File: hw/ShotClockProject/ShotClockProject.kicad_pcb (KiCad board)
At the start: 4 copper layers, 71.8 x 71.8 mm, 113 parts, among them IC1 TP4056-42-ESOP8_Rearanged, J1 Conn_01x06_Pin, J10 USB4120-03-C_REVA, J2 Conn_ST_STDC14, J3 SM03B-SRSS-TB(LF)(SN)(P), J4 Conn_01x02_Pin, J5 Conn_01x03_Pin, J6 Conn_01x06_Pin, J7 Conn_01x06_Pin, J8 Conn_01x06_Pin, J9 Conn_01x06_Pin, Q1 Q_PMOS_SGD, Q2 Q_NPN_BCE, Q3 Q_NPN_BCE, Q4 Q_NPN_BCE, SW1 TK-6580S-1, SW2 SW_SPDT, SW3 TK-6580S-2, SW4 TK-6580S-2, SW5 TK-6580S-2, U1 STM32G070CBTx, U2 LD39015M33R, U3 TPS63000, U4 TPS63000, U5 M74HC14YRM13TR, U6 USBLC6-2SC6, Y1 16MHz

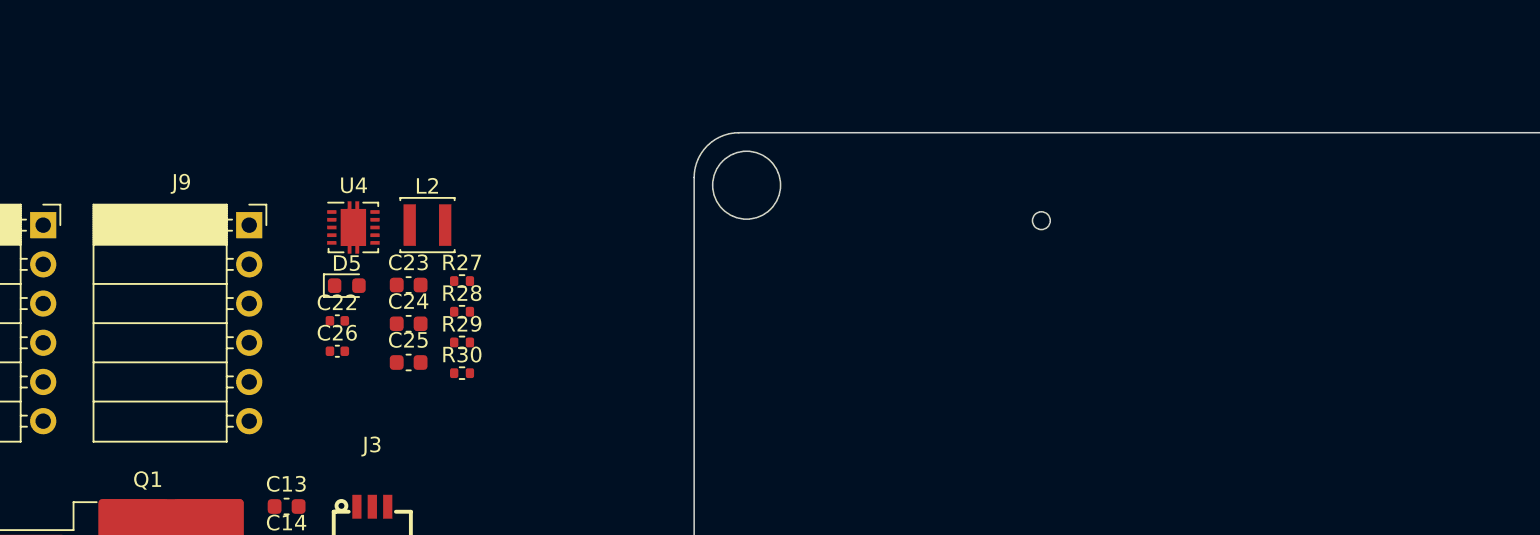
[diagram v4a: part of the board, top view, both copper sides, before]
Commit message: Cleaned second print
and added new connectors, pinout and removed all REV1 stuff.
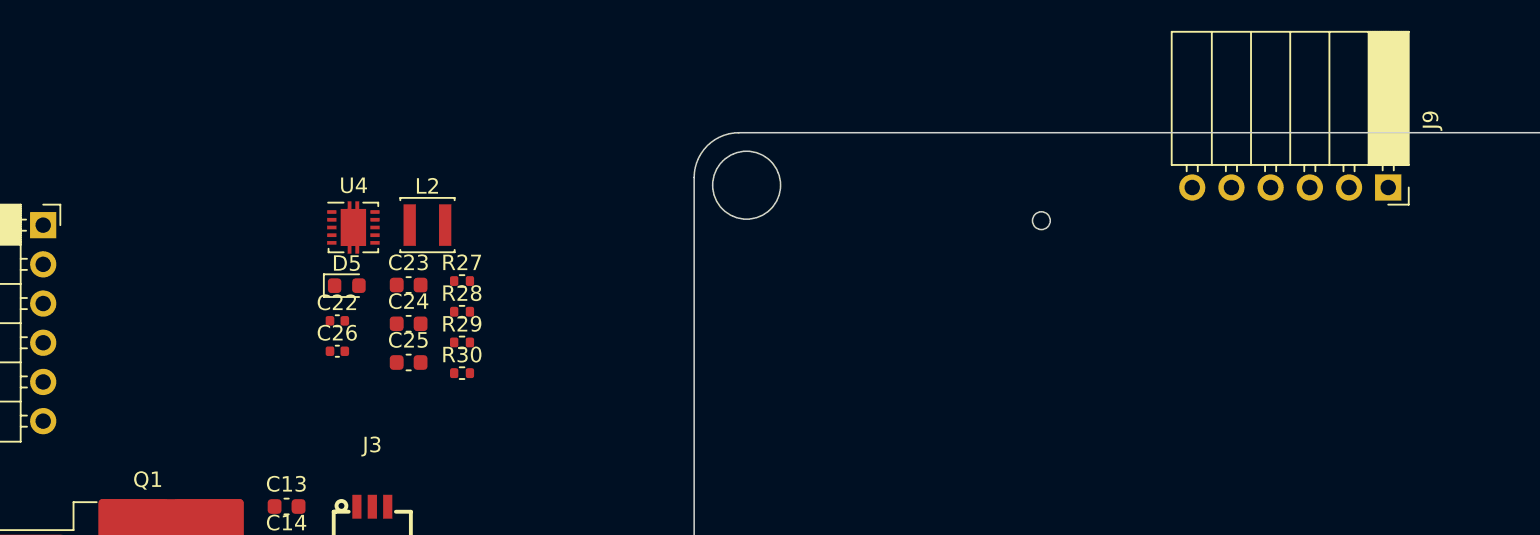
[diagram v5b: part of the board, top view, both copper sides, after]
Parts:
- moved J9 73.8 mm to (163.1, 67.7), turned to -90 degrees
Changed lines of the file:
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@@
   )
   (footprint "Connector_PinSocket_2.54mm:PinSocket_1x06_P2.54mm_Horizontal" (layer "F.Cu")
-    (at 89.27 70.09)
+    (at 163.075 67.65 -90)
     (descr "Through hole angled socket strip, 1x06, 2.54mm pitch, 8.51mm socket length, single row (from Kicad 4.0.7), script generated")
     (tags "Through hole angled socket strip THT 1x06 2.54mm single row")
@@
     (property "ki_keywords" "connector")
     (attr through_hole)
-    (fp_text reference "J9" (at -4.38 -2.77) (layer "F.SilkS")
+    (fp_text reference "J9" (at -4.38 -2.77 90) (layer "F.SilkS")
         (effects (font (size 1 1) (thickness 0.15)))
     )
-    (fp_text value "Conn_01x06_Pin" (at -4.38 15.47) (layer "F.Fab")
+    (fp_text value "Conn_01x06_Pin" (at -4.38 15.47 90) (layer "F.Fab")
         (effects (font (size 1 1) (thickness 0.15)))
     )
-    (fp_text user "${REFERENCE}" (at -5.775 6.35 90) (layer "F.Fab")
+    (fp_text user "${REFERENCE}" (at -5.775 6.35) (layer "F.Fab")
         (effects (font (size 1 1) (thickness 0.15)))
     )
@@
     (fp_line (start 0 13) (end 0 12.4)
       (stroke (width 0.1) (type solid)) (layer "F.Fab"))
-    (pad "1" thru_hole rect (at 0 0) (size 1.7 1.7) (drill 1) (layers "*.Cu" "*.Mask")
+    (pad "1" thru_hole rect (at 0 0 270) (size 1.7 1.7) (drill 1) (layers "*.Cu" "*.Mask")
       (net 53 "TLC59116_RESETn") (pinfunction "Pin_1") (pintype "passive"))
-    (pad "2" thru_hole oval (at 0 2.54) (size 1.7 1.7) (drill 1) (layers "*.Cu" "*.Mask")
+    (pad "2" thru_hole oval (at 0 2.54 270) (size 1.7 1.7) (drill 1) (layers "*.Cu" "*.Mask")
       (net 2 "+3.3V") (pinfunction "Pin_2") (pintype "passive"))
-    (pad "3" thru_hole oval (at 0 5.08) (size 1.7 1.7) (drill 1) (layers "*.Cu" "*.Mask")
+    (pad "3" thru_hole oval (at 0 5.08 270) (size 1.7 1.7) (drill 1) (layers "*.Cu" "*.Mask")
       (net 54 "+5V") (pinfunction "Pin_3") (pintype "passive"))
-    (pad "4" thru_hole oval (at 0 7.62) (size 1.7 1.7) (drill 1) (layers "*.Cu" "*.Mask")
+    (pad "4" thru_hole oval (at 0 7.62 270) (size 1.7 1.7) (drill 1) (layers "*.Cu" "*.Mask")
       (net 55 "I2C1_SCL") (pinfunction "Pin_4") (pintype "passive"))
-    (pad "5" thru_hole oval (at 0 10.16) (size 1.7 1.7) (drill 1) (layers "*.Cu" "*.Mask")
+    (pad "5" thru_hole oval (at 0 10.16 270) (size 1.7 1.7) (drill 1) (layers "*.Cu" "*.Mask")
       (net 56 "I2C1_SDA") (pinfunction "Pin_5") (pintype "passive"))
-    (pad "6" thru_hole oval (at 0 12.7) (size 1.7 1.7) (drill 1) (layers "*.Cu" "*.Mask")
+    (pad "6" thru_hole oval (at 0 12.7 270) (size 1.7 1.7) (drill 1) (layers "*.Cu" "*.Mask")
       (net 4 "GND") (pinfunction "Pin_6") (pintype "passive"))
     (model "${KICAD6_3DMODEL_DIR}/Connector_PinSocket_2.54mm.3dshapes/PinSocket_1x06_P2.54mm_Horizontal.wrl"

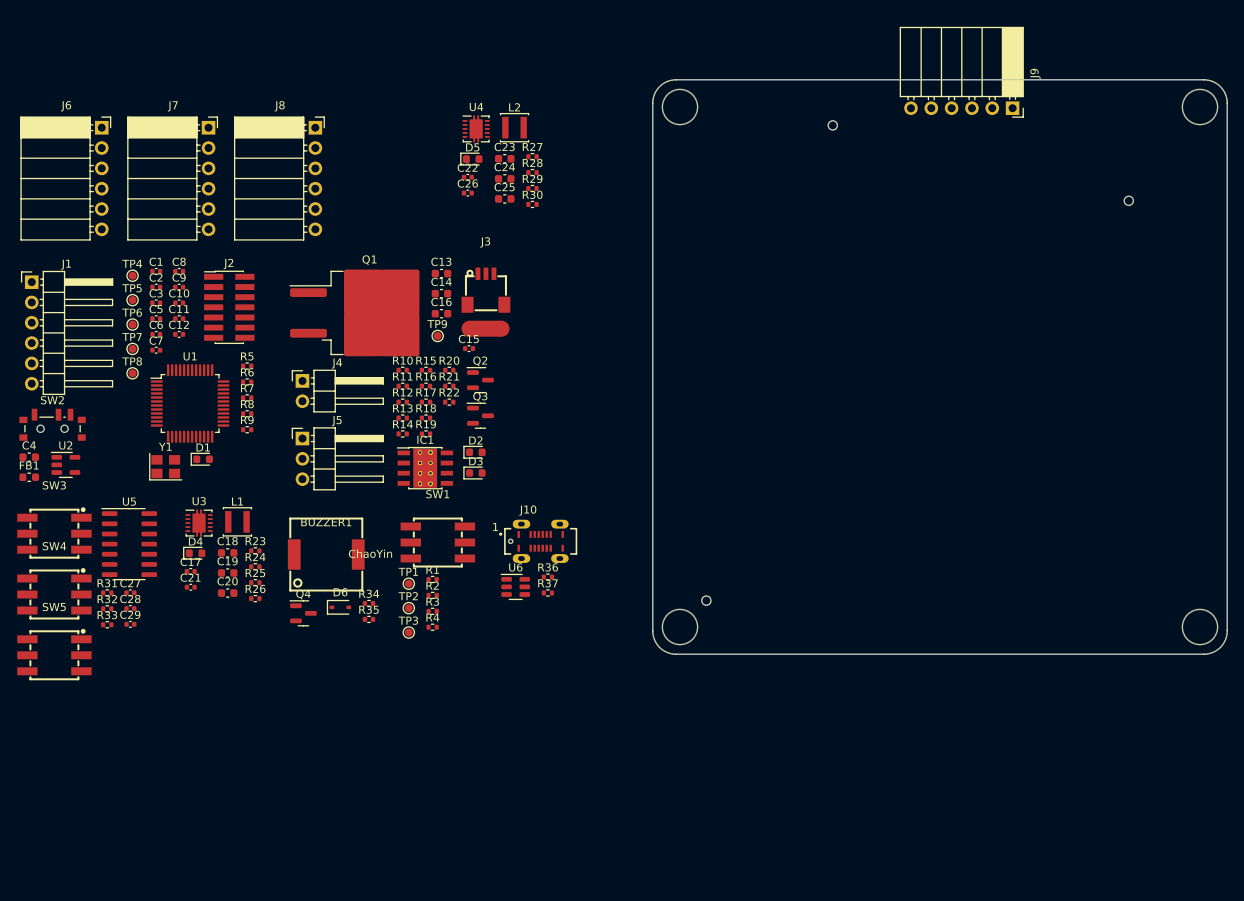
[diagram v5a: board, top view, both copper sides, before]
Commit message: Changed display connectors to JST PH 2.0mm
In docs, schematic and footprints
Both sides, connect with male/male cable
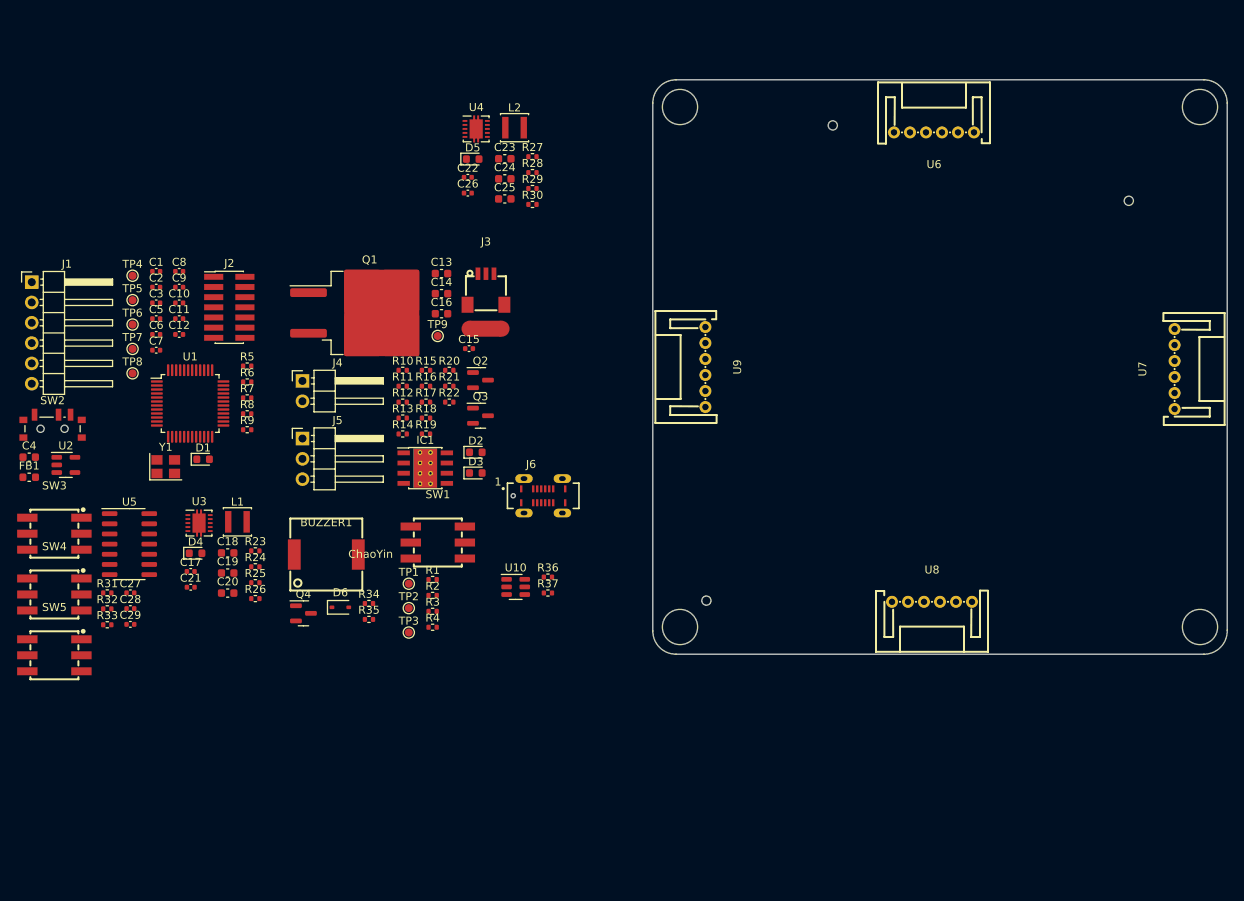
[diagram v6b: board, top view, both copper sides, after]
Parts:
- removed the J6 at (49.2, 70.1)
- removed J7, J8, J9: Conn_01x06_Pin, Connector_PinSocket_2.54mm:PinSocket_1x06_P2.54mm_Horizontal
- added U6: S6B-PH-K-S-(LF)(SN), S6B_PH_K_S_LF_SN:CONN-TH_6P-P2.00_S6B-PH-K-S-LF-SN, F.Cu at (153.2, 70.7)
- added U7: S6B-PH-K-S-(LF)(SN), S6B_PH_K_S_LF_SN:CONN-TH_6P-P2.00_S6B-PH-K-S-LF-SN, F.Cu at (183.3, 100.2)
- added U8: S6B-PH-K-S-(LF)(SN), S6B_PH_K_S_LF_SN:CONN-TH_6P-P2.00_S6B-PH-K-S-LF-SN, F.Cu at (153.0, 129.3)
- added U9: S6B-PH-K-S-(LF)(SN), S6B_PH_K_S_LF_SN:CONN-TH_6P-P2.00_S6B-PH-K-S-LF-SN, F.Cu at (124.7, 100.0)
- moved J6 5.70 mm to (104.4, 116.1)
- renumbered J10 to J6, U6 to U10

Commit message: XTAL, decoup placement & I2C routing
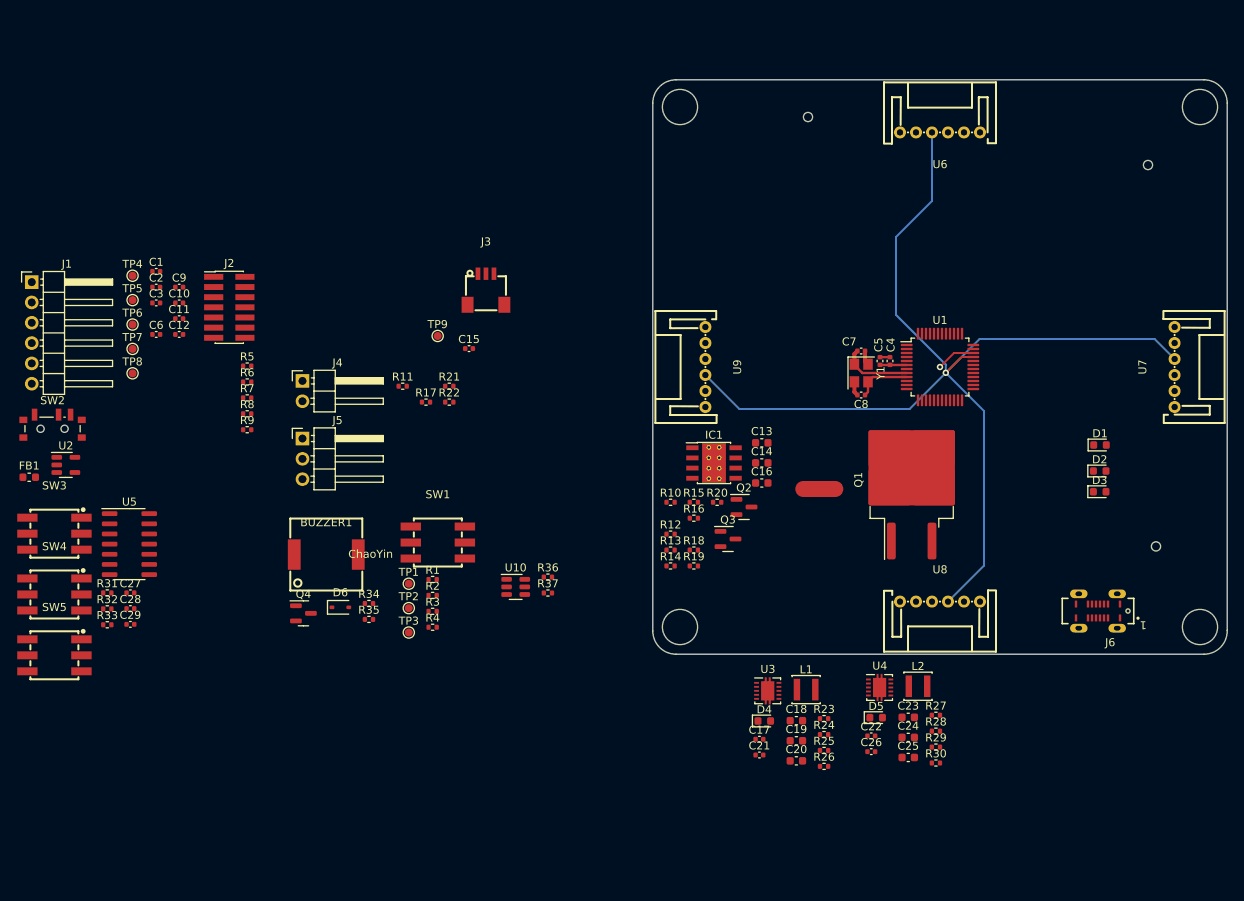
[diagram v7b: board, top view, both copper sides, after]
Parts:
- C4: footprint Capacitor_SMD:C_0603_1608Metric -> Capacitor_SMD:C_0402_1005Metric
- moved D1 112.1 mm to (174.0, 109.8)
- moved C4 108.3 mm to (147.8, 99.2), turned to 90 degrees
- moved U1 93.8 mm to (154.0, 100.0)
- moved C5 90.6 mm to (146.5, 99.2), turned to 90 degrees
- moved C7 88.1 mm to (144.2, 98.0)
- moved Y1 87.7 mm to (144.2, 100.8), turned to -90 degrees
- moved C8 86.6 mm to (144.2, 103.5), turned to 180 degrees
- moved C22 86.1 mm to (145.4, 146.1)
- moved C24 86.1 mm to (150.0, 146.3)
- moved C25 86.1 mm to (150.0, 148.8)
- moved C26 86.1 mm to (145.4, 148.1)
- moved D5 86.1 mm to (146.0, 143.8)
- moved L2 86.1 mm to (151.2, 139.9)
- moved R27 86.1 mm to (153.5, 143.5)
- moved R28 86.1 mm to (153.5, 145.5)
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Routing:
- net I2C1_SCL: track 0.00 -> 135.9 mm, vias 0 -> 1
- net I2C1_SDA: track 0.00 -> 133.2 mm, vias 0 -> 1
- net /STM32G070CBT6/HSE_IN: track 0.00 -> 8.85 mm
- net /STM32G070CBT6/HSE_OUT: track 0.00 -> 6.89 mm
- net GND: track 0.00 -> 4.86 mm
- net +3.3V: track 0.00 -> 3.40 mm
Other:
- outline, holes or cut-outs redrawn

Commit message: Routed V regulators on mainboard
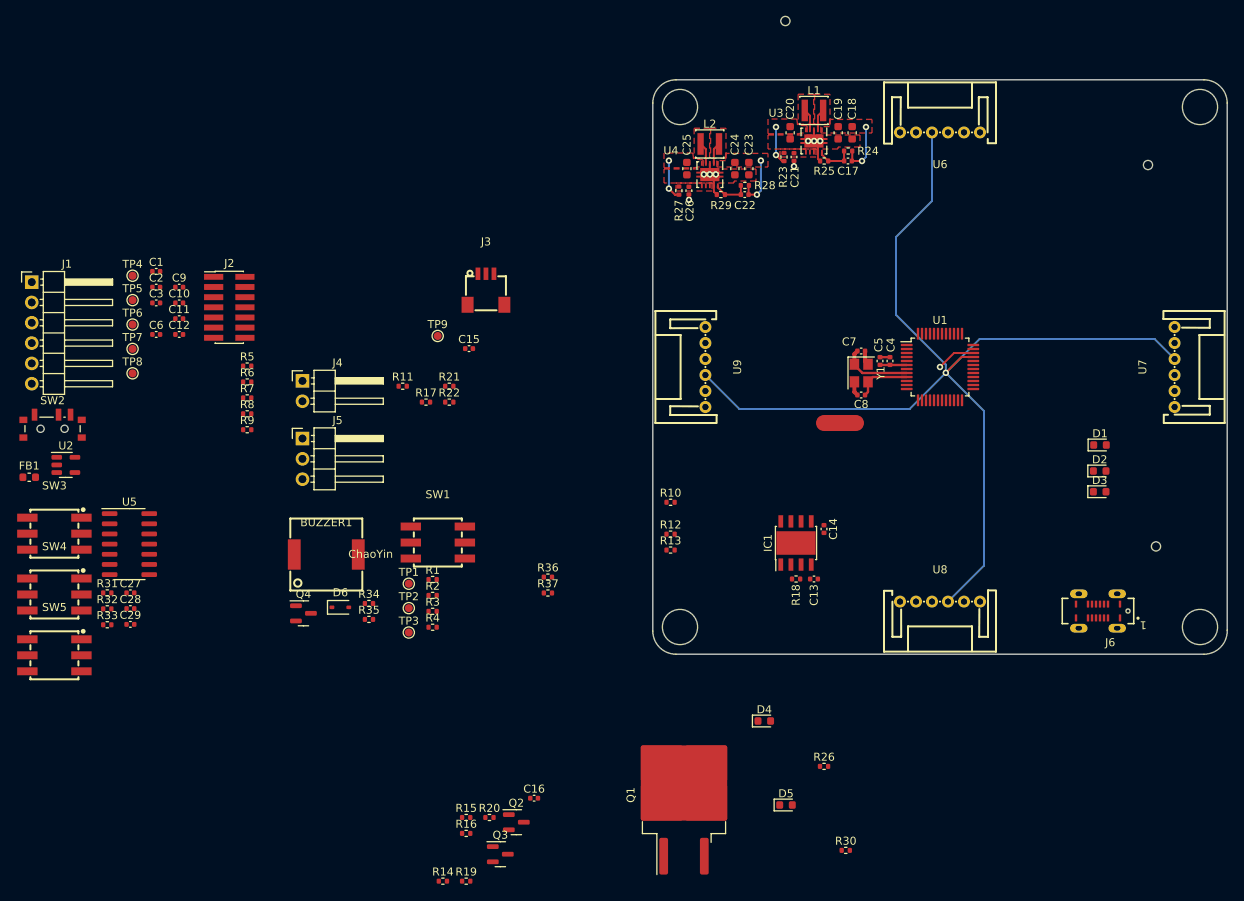
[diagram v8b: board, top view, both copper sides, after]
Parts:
- removed U10: USBLC6-2SC6, Package_TO_SOT_SMD:SOT-23-6
- C13, C14, C16: footprint Capacitor_SMD:C_0603_1608Metric -> Capacitor_SMD:C_0402_1005Metric
- IC1: footprint Package_SO:Texas_HSOP-8-1EP_3.9x4.9mm_P1.27mm_ThermalVias -> Package_SO:Texas_HSOP-8-1EP_3.9x4.9mm_P1.27mm
- U3, U4: footprint Package_SON:Texas_DRC0010J -> Package_SON_Altered:Texas_DRC0010J_Altered
- moved C25 78.6 mm to (122.4, 75.2), turned to -90 degrees
- moved C20 78.5 mm to (135.3, 70.7), turned to -90 degrees
- moved C19 76.2 mm to (141.3, 70.7), turned to -90 degrees
- moved C21 74.9 mm to (135.8, 73.8), turned to -90 degrees
- moved C24 74.3 mm to (128.4, 75.2), turned to -90 degrees
- moved R29 74.1 mm to (126.6, 78.5), turned to 180 degrees
- moved C18 73.8 mm to (143.0, 70.7), turned to -90 degrees
- moved C26 73.7 mm to (122.6, 78.0), turned to -90 degrees
- moved R25 73.7 mm to (139.5, 74.2), turned to 180 degrees
- moved C17 73.1 mm to (142.5, 74.2), turned to 180 degrees
- moved R27 73.0 mm to (121.4, 78.0), turned to 90 degrees
- moved R24 73.0 mm to (142.5, 73.0), turned to 180 degrees
- moved L2 72.6 mm to (125.2, 72.1)
- moved L1 72.4 mm to (138.2, 67.9)
- moved R28 72.3 mm to (129.6, 77.3), turned to 180 degrees
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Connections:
- net /Voltage regulator 3v3/3v3_out renamed /Voltage regulator 3v3/VOUT
- net /Voltage regulator 3v3/batt_in renamed /Voltage regulator 3v3/VIN
- net /Voltage regulator 5V/5v_out renamed /Voltage regulator 5V/VOUT
- net /Voltage regulator 5V/batt_in renamed /Voltage regulator 5V/VIN
- net Net-(D2-A) renamed /Li-Po Battery and charger/VCC
- net Net-(U3-EN) renamed /Voltage regulator 3v3/EN
- net Net-(U3-FB) renamed /Voltage regulator 3v3/FB
- net Net-(U3-L1) renamed /Voltage regulator 3v3/L1
- net Net-(U3-L2) renamed /Voltage regulator 3v3/L2
- net Net-(U4-EN) renamed /Voltage regulator 5V/EN
- net Net-(U4-FB) renamed /Voltage regulator 5V/FB
- net Net-(U4-L1) renamed /Voltage regulator 5V/L1
- net Net-(U4-L2) renamed /Voltage regulator 5V/L2
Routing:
- net GND: track 4.86 -> 16.8 mm, vias 0 -> 8
- net /Voltage regulator 3v3/VOUT: track 0.00 -> 6.70 mm, vias 0 -> 2
- net /Voltage regulator 5V/VOUT: track 0.00 -> 6.66 mm, vias 0 -> 2
- net /Voltage regulator 5V/VIN: track 0.00 -> 5.06 mm, vias 0 -> 2
- net /Voltage regulator 3v3/VIN: track 0.00 -> 4.81 mm, vias 0 -> 2
- net /Voltage regulator 5V/FB: track 0.00 -> 4.61 mm
- net /Voltage regulator 3v3/FB: track 0.00 -> 4.41 mm
- net /Voltage regulator 5V/L1: track 0.00 -> 2.71 mm
- net /Voltage regulator 5V/L2: track 0.00 -> 2.70 mm
- net /Voltage regulator 3v3/L2: track 0.00 -> 2.69 mm
- net /Voltage regulator 3v3/L1: track 0.00 -> 2.68 mm
- added copper zone on F.Cu, net /Voltage regulator 3v3/EN
- added copper zone on F.Cu, net /Voltage regulator 3v3/L1
- added copper zone on F.Cu, net /Voltage regulator 3v3/L2
- added copper zone on F.Cu, net /Voltage regulator 3v3/VIN
- added copper zone on F.Cu, net /Voltage regulator 3v3/VOUT
- added copper zone on F.Cu, net /Voltage regulator 5V/EN
- added copper zone on F.Cu, net /Voltage regulator 5V/L1
- added copper zone on F.Cu, net /Voltage regulator 5V/L2
- added copper zone on F.Cu, net /Voltage regulator 5V/VIN
- added copper zone on F.Cu, net /Voltage regulator 5V/VOUT
- added copper zone on F.Cu, net GND
- added copper zone on In1.Cu, net GND
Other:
- board size 71.8 x 71.8 mm -> 71.8 x 79.7 mm
